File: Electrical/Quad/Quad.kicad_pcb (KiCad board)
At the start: 2 copper layers, 140 x 70 mm, 117 parts, among them J101 01x04, J102 02x04, J103 01x04, J104 01x03, J105 01x03, J106 01x03, J107 01x03, J108 01x03, J109 01x03, J110 01x04, J111 01x04, J112 01x04, J113 01x04, J114 01x03, J115 01x03, J116 01x03, J117 01x03, J201 01x02, J202 01x04, J203 01x03, J204 01x04, J205 01x03, J206 USB_OTG, J207 01x04, J208 01x02, J209 01x04, J210 01x02, J211 01x02, J212 4PostTerm, J213 2PostTerm, J214 2PostTerm, J215 JST_3, J216 2PostTerm, J217 2PostTerm, Q201 FDC6420C, Q202 FDG1024NZ, Q301 FDC6420C, Q401 FDC6420C, U201 TPD4S012, U202 ACS712ELCTR-05B-T, U203 ACS712ELCTR-05B-T, U204 24LC256, U205 LM2576HVS-ADJ, U206 LM2576HVS-ADJ

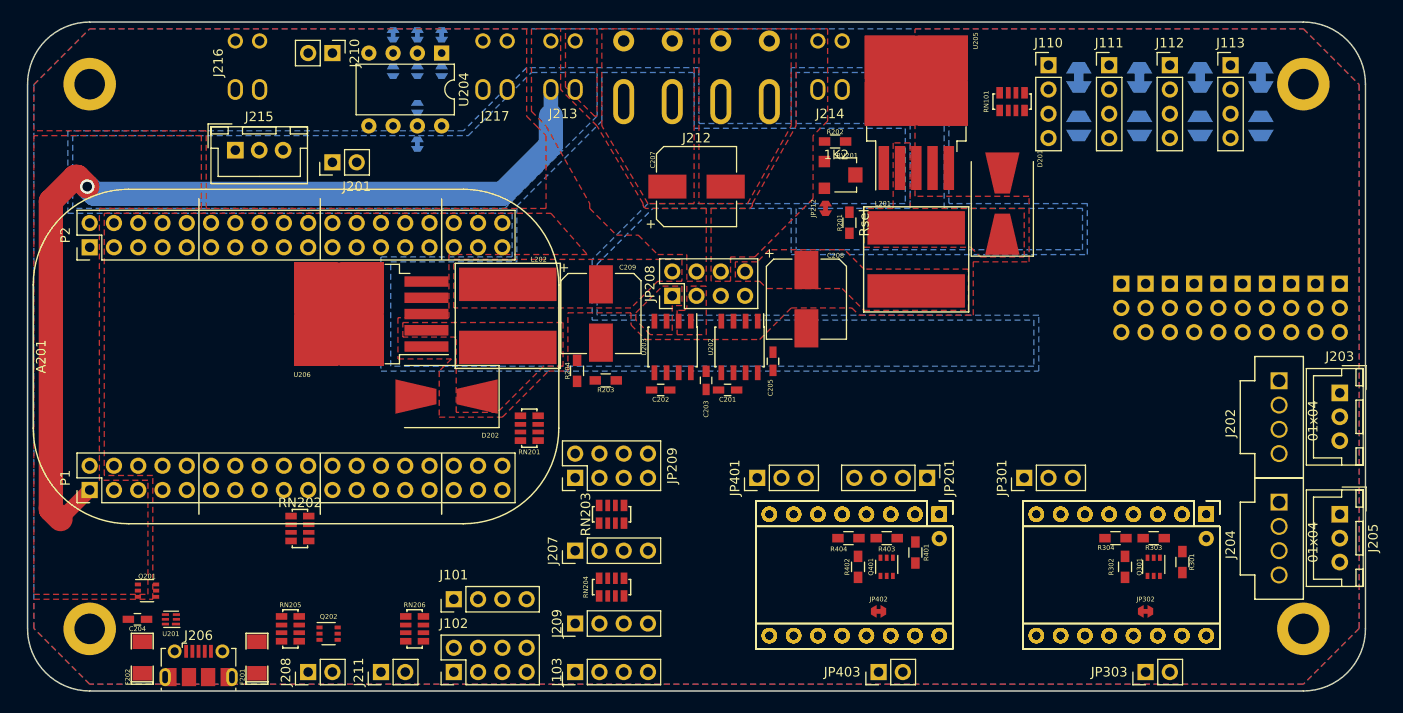
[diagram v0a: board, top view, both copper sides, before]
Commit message: Completed Quad stepper version of the board.
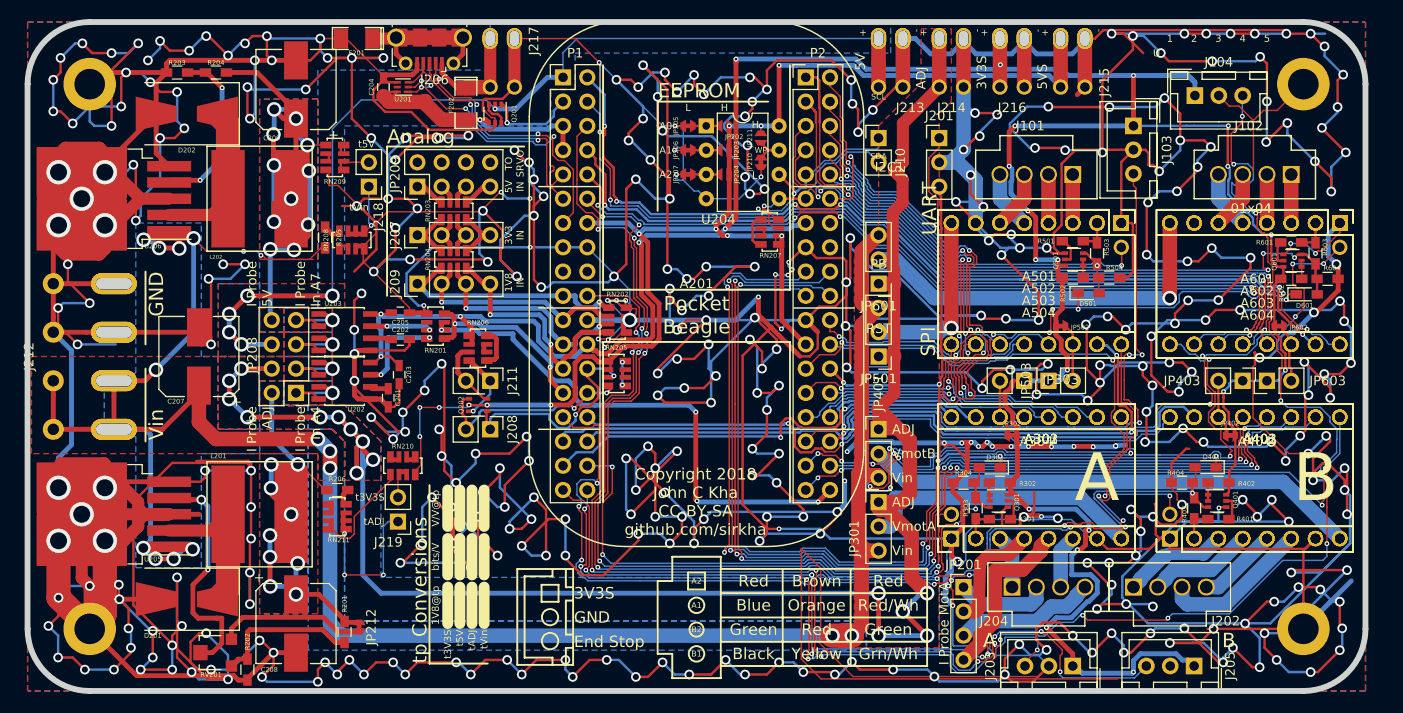
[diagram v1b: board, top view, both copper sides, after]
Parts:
- removed J105, J106, J107, J108, J109, J114, J115, J116, J117: 01x03, footprints:Pin_Header_Straight_1x03_Pitch2.54mm_Blank
- removed J110, J111, J112, J113: 01x04, Pin_Headers:Pin_Header_Straight_1x04_Pitch2.54mm
- removed JP101, JP102, JP103, JP104: JPNC, footprints:JPNC_Large
- removed JP105, JP106, JP107, JP108: JPNO, footprints:JPNO_Large
- removed RN101: 1K2, footprints:R_Array_1206x04
- added A501: Pololu_Breakout_A4988, footprints:Pololu_Breakout-16_15.2x20.3mm, F.Cu at (144.4, 86.0)
- added A502: Pololu_Breakout_DRV8825, footprints:Pololu_Breakout-16_15.2x20.3mm, F.Cu at (144.4, 86.0)
- added A503: Pololu_Breakout_DRV8834, footprints:Pololu_Breakout-16_15.2x20.3mm, F.Cu at (144.4, 86.0)
- added A504: Pololu_Breakout_DRV8880, footprints:Pololu_Breakout-17_15.2x20.3mm, F.Cu at (144.4, 86.0)
- added A601: Pololu_Breakout_A4988, footprints:Pololu_Breakout-16_15.2x20.3mm, F.Cu at (167.3, 86.0)
- added A602: Pololu_Breakout_DRV8825, footprints:Pololu_Breakout-16_15.2x20.3mm, F.Cu at (167.3, 86.0)
- added A603: Pololu_Breakout_DRV8834, footprints:Pololu_Breakout-16_15.2x20.3mm, F.Cu at (167.3, 86.0)
- added A604: Pololu_Breakout_DRV8880, footprints:Pololu_Breakout-17_15.2x20.3mm, F.Cu at (167.3, 86.0)
- added D301: D, footprints:D_0603_HandSoldering, F.Cu at (130.7, 111.6)
- added D401: D, footprints:D_0603_HandSoldering, F.Cu at (153.3, 111.6)
- added D501: D, footprints:D_0603_HandSoldering, F.Cu at (141.0, 93.4)
- added D601: D, footprints:D_0603_HandSoldering, F.Cu at (163.8, 93.5)
- added J218: 01x02, Pin_Headers:Pin_Header_Straight_1x02_Pitch2.54mm, F.Cu at (65.7, 82.2)
- added J219: 01x02, Pin_Headers:Pin_Header_Straight_1x02_Pitch2.54mm, F.Cu at (68.8, 117.3)
- added JP501: 01x03, Pin_Headers:Pin_Header_Straight_1x03_Pitch2.54mm, F.Cu at (119.0, 100.0)
- added JP502: JPNC, footprints:JPNC, F.Cu at (138.1, 96.8)
- added JP503: 01x02, Pin_Headers:Pin_Header_Straight_1x02_Pitch2.54mm, F.Cu at (136.8, 102.5)
- added JP601: 01x03, Pin_Headers:Pin_Header_Straight_1x03_Pitch2.54mm, F.Cu at (119.0, 92.4)
- added JP602: JPNC, footprints:JPNC, F.Cu at (161.0, 96.8)
- added JP603: 01x02, Pin_Headers:Pin_Header_Straight_1x02_Pitch2.54mm, F.Cu at (159.7, 102.5)
- added Q501: FDC6420C, TO_SOT_Packages_SMD:SOT-363_SC-70-6, F.Cu at (139.5, 89.8)
- added Q601: FDC6420C, TO_SOT_Packages_SMD:SOT-363_SC-70-6, F.Cu at (162.4, 90.0)
- added R205: 12K, Resistors_SMD:R_0603_HandSoldering, F.Cu at (61.1, 87.6)
- added R206: 12K, Resistors_SMD:R_0603_HandSoldering, F.Cu at (62.4, 114.0)
- added R501: 22, Resistors_SMD:R_0603_HandSoldering, F.Cu at (139.4, 87.9)
- added R502: 12K, Resistors_SMD:R_0603_HandSoldering, F.Cu at (139.4, 91.7)
- added R503: 1K2, Resistors_SMD:R_0603_HandSoldering, F.Cu at (141.9, 89.2)
- added R504: 12K, Resistors_SMD:R_0603_HandSoldering, F.Cu at (143.2, 91.7)
- added R601: 22, Resistors_SMD:R_0603_HandSoldering, F.Cu at (162.2, 88.1)
- added R602: 12K, Resistors_SMD:R_0603_HandSoldering, F.Cu at (162.2, 91.9)
- added R603: 1K2, Resistors_SMD:R_0603_HandSoldering, F.Cu at (164.8, 89.2)
- added R604: 12K, Resistors_SMD:R_0603_HandSoldering, F.Cu at (166.0, 91.9)
- added RN207: 1K2, footprints:R_Array_1206x04, F.Cu at (107.7, 87.0)
- added RN208: 1K2, footprints:R_Array_1206x04, F.Cu at (63.9, 87.8)
- added RN209: 1K2, footprints:R_Array_1206x04, F.Cu at (62.2, 79.2)
- added RN210: 1K2, footprints:R_Array_1206x04, F.Cu at (69.3, 111.4)
- added RN211: 1K2, footprints:R_Array_1206x04, F.Cu at (62.4, 116.8)
- A301, A302, A303, A401, A402, A403: footprint Modules:Pololu_Breakout-16_15.2x20.3mm -> footprints:Pololu_Breakout-16_15.2x20.3mm
- J101: footprint Pin_Headers:Pin_Header_Straight_1x04_Pitch2.54mm -> footprints:Molex-SL-4POS
- J102: value 02x04 -> 01x04; footprint Pin_Headers:Pin_Header_Straight_2x04_Pitch2.54mm -> footprints:Molex-SL-4POS
- J103: value 01x04 -> 01x03; footprint Pin_Headers:Pin_Header_Straight_1x04_Pitch2.54mm -> Connectors_JST:JST_XH_B03B-XH-A_03x2.50mm_Straight
- J104: footprint footprints:Pin_Header_Straight_1x03_Pitch2.54mm_Blank -> Connectors_JST:JST_XH_B03B-XH-A_03x2.50mm_Straight
- J201: value 01x02 -> 01x03; footprint Pin_Headers:Pin_Header_Straight_1x02_Pitch2.54mm -> Pin_Headers:Pin_Header_Straight_1x03_Pitch2.54mm
- J206: footprint Connectors_USB:USB_Micro-B_Molex-105017-0001 -> footprints:USB_Micro-B_Molex-105017-0001_CircularHoles
- J213, J214, J216, J217, JP202, JP203, JP204, JP205, JP206, JP207, JP210, JP211: moved to F.Cu
- J215: value JST_3 -> 2PostTerm; footprint Connectors_JST:JST_XH_B03B-XH-A_03x2.50mm_Straight -> footprints:TerminalBlock_Custom_1x02.54mm
- moved J102 101.9 mm to (162.2, 81.0), turned to 0 degrees
- moved D201 94.9 mm to (46.7, 125.4), turned to 180 degrees
- moved U205 93.9 mm to (39.0, 116.5), turned to 180 degrees
- moved J215 88.1 mm to (139.4, 69.3)
- moved R202 82.7 mm to (53.0, 132.8), turned to 90 degrees
- moved RV201 82.2 mm to (49.7, 131.0), turned to 90 degrees
- moved J103 81.7 mm to (145.7, 75.9), turned to 270 degrees
- moved J216 80.0 mm to (133.0, 69.3)
- moved J101 78.6 mm to (139.4, 81.0), turned to 0 degrees
- moved L201 73.7 mm to (54.3, 116.5), turned to 0 degrees
- moved J206 70.5 mm to (72.1, 67.0), turned to 180 degrees
- moved J212 69.9 mm to (36.5, 100.0), turned to 270 degrees
- moved R201 68.0 mm to (63.2, 128.8), turned to 270 degrees
- moved F202 67.1 mm to (75.9, 73.6), turned to 270 degrees
- moved A201 65.7 mm to (86.0, 70.8), turned to 0 degrees
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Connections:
- net /Common/usb1_dn renamed /Common/usb1_d-
- net /Common/usb1_dp renamed /Common/usb1_d+
- A201 pad 1.10: /ehrpwm0B -> /gpio0_3
- A201 pad 1.17: Net-(A201-Pad1.17) -> (no net)
- A201 pad 1.18: Net-(A201-Pad1.18) -> (no net)
- A201 pad 1.2: /gpio2_23 -> /pr1_pru1_pru_r30_09
- A201 pad 1.4: /gpio2_25 -> /pr1_pru1_pru_r30_11
- A201 pad 1.8: /ehrpwm0A -> /gpio0_2
- A201 pad 2.1: /ehrpwm1A -> /gpio1_18
- A201 pad 2.10: /Common/gpio1_20 -> /gpio1_20
- A201 pad 2.14: +BATT -> (no net)
- A201 pad 2.16: /Common/batt_temp -> (no net)
- A201 pad 2.24: /gpio1_12 -> /Common/gpio1_12
- A201 pad 2.25: /spi1_d1 -> /gpio1_9
- A201 pad 2.26: Net-(A201-Pad2.26) -> RST
- A201 pad 2.27: /spi1_d0 -> /gpio1_8
- A201 pad 2.28: /gpio3_20 -> /pr1_pru0_pru_r30_06
- A201 pad 2.29: /spi1_sclk -> /gpio0_7
- A201 pad 2.3: /ehrpwm2B -> /gpio0_23
- A201 pad 2.30: /gpio3_17 -> /pr1_pru0_pru_r31_03
- A201 pad 2.31: /spi1_cs1 -> /gpio0_19
- A201 pad 2.32: /gpio3_16 -> /pr1_pru0_pru_r30_02
- A201 pad 2.33: /gpio1_13 -> /pr1_pu0_pru_r30_15
- A201 pad 2.34: /gpio3_19 -> /pr1_pru0_pru_r30_05
- A201 pad 2.35: /gpio2_22 -> /pr1_pru1_pru_r31_08
- A201 pad 2.5: /uart4_rxd -> /gpio0_30
- A201 pad 2.7: /uart4_txd -> /gpio0_31
- A301 pad 10: /Common/gpio2_0 -> /Common/gpio1_27
- A301 pad 11: /Common/gpio0_27 -> /Common/gpio1_26
- A301 pad 12: /Common/gpio1_15 -> /Common/gpio1_25
- A301 pad 13: /Common/gpio2_1 -> /Common/gpio1_28
- A301 pad 14: /Common/StepperB/SLP -> /Common/StepperA/SLP
- A301 pad 15: /Common/pr1_pru1_pru_r30_15 -> /Common/pr1_pru0_pru_r30_04
- A301 pad 16: /Common/pr1_pru1_pru_r30_14 -> /Common/pr1_pru0_pru_r30_01
- A301 pad 2: /Common/StepperB/fault_supply -> /Common/StepperA/fault_supply
- A301 pad 3: /Common/StepperB/A2 -> /Common/StepperA/A2
- A301 pad 4: /Common/StepperB/A1 -> /Common/StepperA/A1
- A301 pad 5: /Common/StepperB/B1 -> /Common/StepperA/B1
- A301 pad 6: /Common/StepperB/B2 -> /Common/StepperA/B2
- A301 pad 8: /Common/StepperB/Vmot -> /Common/StepperA/Vmot
- A301 pad 9: /Common/pr1_pru0_pru_r30_00 -> /Common/pr1_pru0_pru_r30_07
- A302 pad 10: /Common/gpio2_0 -> /Common/gpio1_27
- A302 pad 11: /Common/gpio0_27 -> /Common/gpio1_26
- A302 pad 12: /Common/gpio1_15 -> /Common/gpio1_25
- A302 pad 13: /Common/gpio2_1 -> /Common/gpio1_28
- A302 pad 14: /Common/StepperB/SLP -> /Common/StepperA/SLP
- A302 pad 15: /Common/pr1_pru1_pru_r30_15 -> /Common/pr1_pru0_pru_r30_04
- A302 pad 16: /Common/pr1_pru1_pru_r30_14 -> /Common/pr1_pru0_pru_r30_01
- A302 pad 2: /Common/StepperB/fault_supply -> /Common/StepperA/fault_supply
- A302 pad 3: /Common/StepperB/A2 -> /Common/StepperA/A2
- A302 pad 4: /Common/StepperB/A1 -> /Common/StepperA/A1
- A302 pad 5: /Common/StepperB/B1 -> /Common/StepperA/B1
- A302 pad 6: /Common/StepperB/B2 -> /Common/StepperA/B2
- A302 pad 8: /Common/StepperB/Vmot -> /Common/StepperA/Vmot
- A302 pad 9: /Common/pr1_pru0_pru_r30_00 -> /Common/pr1_pru0_pru_r30_07
- A303 pad 10: /Common/gpio2_0 -> /Common/gpio1_27
- A303 pad 11: /Common/gpio0_27 -> /Common/gpio1_26
- A303 pad 12: /Common/gpio1_15 -> /Common/gpio1_25
- A303 pad 13: /Common/gpio2_1 -> /Common/gpio1_28
- A303 pad 14: /Common/StepperB/SLP -> /Common/StepperA/SLP
- A303 pad 15: /Common/pr1_pru1_pru_r30_15 -> /Common/pr1_pru0_pru_r30_04
- A303 pad 16: /Common/pr1_pru1_pru_r30_14 -> /Common/pr1_pru0_pru_r30_01
- A303 pad 2: /Common/StepperB/fault_supply -> /Common/StepperA/fault_supply
- A303 pad 3: /Common/StepperB/A2 -> /Common/StepperA/A2
- A303 pad 4: /Common/StepperB/A1 -> /Common/StepperA/A1
- A303 pad 5: /Common/StepperB/B1 -> /Common/StepperA/B1
- A303 pad 6: /Common/StepperB/B2 -> /Common/StepperA/B2
- A303 pad 8: /Common/StepperB/Vmot -> /Common/StepperA/Vmot
- A303 pad 9: /Common/pr1_pru0_pru_r30_00 -> /Common/pr1_pru0_pru_r30_07
- A304 pad 10: /Common/gpio2_0 -> /Common/gpio1_27
- A304 pad 11: /Common/gpio0_27 -> /Common/gpio1_26
- A304 pad 12: /Common/gpio1_15 -> /Common/gpio1_25
- A304 pad 13: /Common/gpio2_1 -> /Common/gpio1_28
- A304 pad 14: /Common/StepperB/SLP -> /Common/StepperA/SLP
- A304 pad 15: /Common/pr1_pru1_pru_r30_15 -> /Common/pr1_pru0_pru_r30_04
- A304 pad 16: /Common/pr1_pru1_pru_r30_14 -> /Common/pr1_pru0_pru_r30_01
- A304 pad 17: /Common/gpio1_28 -> /Common/gpio0_26
- A304 pad 2: /Common/StepperB/fault_supply -> /Common/StepperA/fault_supply
- A304 pad 3: /Common/StepperB/A2 -> /Common/StepperA/A2
- A304 pad 4: /Common/StepperB/A1 -> /Common/StepperA/A1
- A304 pad 5: /Common/StepperB/B1 -> /Common/StepperA/B1
- A304 pad 6: /Common/StepperB/B2 -> /Common/StepperA/B2
- A304 pad 8: /Common/StepperB/Vmot -> /Common/StepperA/Vmot
- A304 pad 9: /Common/pr1_pru0_pru_r30_00 -> /Common/pr1_pru0_pru_r30_07
- A401 pad 10: /Common/gpio1_27 -> /Common/gpio2_0
- A401 pad 11: /Common/gpio1_26 -> /Common/gpio0_27
- A401 pad 12: /Common/gpio1_25 -> /Common/gpio1_15
- A401 pad 13: /Common/gpio1_20 -> /Common/gpio2_1
- A401 pad 14: /Common/StepperA/SLP -> /Common/StepperB/SLP
- A401 pad 15: /Common/pr1_pru0_pru_r30_04 -> /Common/pr1_pru1_pru_r30_14
- A401 pad 16: /Common/pr1_pru0_pru_r30_01 -> /Common/pr1_pru1_pru_r30_15
- A401 pad 2: /Common/StepperA/fault_supply -> /Common/StepperB/fault_supply
- A401 pad 3: /Common/StepperA/A2 -> /Common/StepperB/A2
- A401 pad 4: /Common/StepperA/A1 -> /Common/StepperB/A1
- A401 pad 5: /Common/StepperA/B1 -> /Common/StepperB/B1
- A401 pad 6: /Common/StepperA/B2 -> /Common/StepperB/B2
- A401 pad 8: /Common/StepperA/Vmot -> /Common/StepperB/Vmot
- A401 pad 9: /Common/pr1_pru0_pru_r30_07 -> /Common/pr1_pru0_pru_r30_00
- A402 pad 10: /Common/gpio1_27 -> /Common/gpio2_0
- A402 pad 11: /Common/gpio1_26 -> /Common/gpio0_27
- A402 pad 12: /Common/gpio1_25 -> /Common/gpio1_15
- A402 pad 13: /Common/gpio1_20 -> /Common/gpio2_1
- A402 pad 14: /Common/StepperA/SLP -> /Common/StepperB/SLP
- A402 pad 15: /Common/pr1_pru0_pru_r30_04 -> /Common/pr1_pru1_pru_r30_14
- A402 pad 16: /Common/pr1_pru0_pru_r30_01 -> /Common/pr1_pru1_pru_r30_15
- A402 pad 2: /Common/StepperA/fault_supply -> /Common/StepperB/fault_supply
- A402 pad 3: /Common/StepperA/A2 -> /Common/StepperB/A2
- A402 pad 4: /Common/StepperA/A1 -> /Common/StepperB/A1
- A402 pad 5: /Common/StepperA/B1 -> /Common/StepperB/B1
- A402 pad 6: /Common/StepperA/B2 -> /Common/StepperB/B2
- A402 pad 8: /Common/StepperA/Vmot -> /Common/StepperB/Vmot
- A402 pad 9: /Common/pr1_pru0_pru_r30_07 -> /Common/pr1_pru0_pru_r30_00
- A403 pad 10: /Common/gpio1_27 -> /Common/gpio2_0
- A403 pad 11: /Common/gpio1_26 -> /Common/gpio0_27
- A403 pad 12: /Common/gpio1_25 -> /Common/gpio1_15
- A403 pad 13: /Common/gpio1_20 -> /Common/gpio2_1
- A403 pad 14: /Common/StepperA/SLP -> /Common/StepperB/SLP
- A403 pad 15: /Common/pr1_pru0_pru_r30_04 -> /Common/pr1_pru1_pru_r30_14
- A403 pad 16: /Common/pr1_pru0_pru_r30_01 -> /Common/pr1_pru1_pru_r30_15
- A403 pad 2: /Common/StepperA/fault_supply -> /Common/StepperB/fault_supply
- A403 pad 3: /Common/StepperA/A2 -> /Common/StepperB/A2
- A403 pad 4: /Common/StepperA/A1 -> /Common/StepperB/A1
- A403 pad 5: /Common/StepperA/B1 -> /Common/StepperB/B1
- A403 pad 6: /Common/StepperA/B2 -> /Common/StepperB/B2
- A403 pad 8: /Common/StepperA/Vmot -> /Common/StepperB/Vmot
- A403 pad 9: /Common/pr1_pru0_pru_r30_07 -> /Common/pr1_pru0_pru_r30_00
- A404 pad 10: /Common/gpio1_27 -> /Common/gpio2_0
- A404 pad 11: /Common/gpio1_26 -> /Common/gpio0_27
- A404 pad 12: /Common/gpio1_25 -> /Common/gpio1_15
- A404 pad 13: /Common/gpio1_20 -> /Common/gpio2_1
- A404 pad 14: /Common/StepperA/SLP -> /Common/StepperB/SLP
- A404 pad 15: /Common/pr1_pru0_pru_r30_04 -> /Common/pr1_pru1_pru_r30_14
- A404 pad 16: /Common/pr1_pru0_pru_r30_01 -> /Common/pr1_pru1_pru_r30_15
- A404 pad 17: /Common/gpio0_26 -> /Common/gpio1_12
- A404 pad 2: /Common/StepperA/fault_supply -> /Common/StepperB/fault_supply
- A404 pad 3: /Common/StepperA/A2 -> /Common/StepperB/A2
- A404 pad 4: /Common/StepperA/A1 -> /Common/StepperB/A1
- A404 pad 5: /Common/StepperA/B1 -> /Common/StepperB/B1
- A404 pad 6: /Common/StepperA/B2 -> /Common/StepperB/B2
- A404 pad 8: /Common/StepperA/Vmot -> /Common/StepperB/Vmot
- A404 pad 9: /Common/pr1_pru0_pru_r30_07 -> /Common/pr1_pru0_pru_r30_00
- C204 pad 1: Net-(C204-Pad1) -> /Common/usb1_vbus
- F202 pad 1: Net-(F202-Pad1) -> /Common/usb1_5V
- F202 pad 2: Net-(C204-Pad1) -> /Common/usb1_vbus
- J101 pad 1: GND -> /StepperC/A2
- J101 pad 2: /uart4_txd -> /StepperC/A1
- J101 pad 3: /uart4_rxd -> /StepperC/B2
- J101 pad 4: 3V3S -> /StepperC/B1
- J102 pad 1: /spi1_d1 -> /StepperD/A2
- J102 pad 2: 3V3S -> /StepperD/A1
- J102 pad 3: /spi1_cs1 -> /StepperD/B2
- J102 pad 4: GND -> /StepperD/B1
- J103 pad 1: /ehrpwm2B -> 3V3S
- J103 pad 2: /ehrpwm1A -> GND
- J103 pad 3: /ehrpwm0B -> /pr1_pru0_pru_r31_03
- J104 pad 1: GND -> 3V3S
- J104 pad 2: 3V3S -> GND
- J104 pad 3: /gpio1_12 -> /pr1_pru1_pru_r31_08
- J201 pad 2: Net-(A201-Pad2.26) -> GND
- J206 pad 1: Net-(F202-Pad1) -> /Common/usb1_5V
- J208 pad 1: /Common/i2c2_scl -> /Common/i2c2_sda
- J208 pad 2: /Common/i2c2_sda -> /Common/i2c2_scl
- J210 pad 1: /Common/i2c1_sda -> /Common/i2c1_scl
- J210 pad 2: /Common/i2c1_scl -> /Common/i2c1_sda
- J215 pad 1: +BATT -> 5VS
- J215 pad 2: /Common/batt_temp -> GND
- J216 pad 1: 5VS -> 3V3S
- J217 pad 1: 3V3S -> /Common/usb1_5V
- JP208 pad b1: /Common/IP_5V -> /Common/IP_vadj
- JP208 pad b2: +5V -> Vadj
- JP208 pad b3: Vadj -> +5V
- JP208 pad b4: /Common/IP_vadj -> /Common/IP_5V
- JP209 pad b1: /ain_0 -> GND
- JP209 pad b2: /ain_1 -> GND
- JP209 pad b3: /ain_2 -> GND
- JP209 pad b4: /ain_3 -> GND
- JP301 pad 1: Vin -> Vadj
- JP301 pad 2: /Common/StepperB/Vmot -> /Common/StepperA/Vmot
- JP301 pad 3: Vadj -> Vin
- JP302 pad 1: /Common/StepperB/SLP -> /Common/StepperA/SLP
- JP303 pad 2: /Common/StepperB/SLP -> /Common/StepperA/SLP
- JP401 pad 1: Vin -> Vadj
- JP401 pad 2: /Common/StepperA/Vmot -> /Common/StepperB/Vmot
- JP401 pad 3: Vadj -> Vin
- JP402 pad 1: /Common/StepperA/SLP -> /Common/StepperB/SLP
- JP403 pad 2: /Common/StepperA/SLP -> /Common/StepperB/SLP
- Q201 pad 4: Net-(C204-Pad1) -> /Common/usb1_vbus
- Q202 pad 3: Net-(J211-Pad2) -> Net-(J211-Pad1)
- Q202 pad 6: Net-(J211-Pad1) -> Net-(J211-Pad2)
- Q301 pad 3: /Common/gpio0_4 -> /Common/gpio0_5
- Q401 pad 3: /Common/gpio0_5 -> /Common/gpio0_4
- R301 pad 1: /Common/StepperB/fault_supply -> /Common/StepperA/fault_supply
- R303 pad 1: /Common/gpio0_4 -> /Common/gpio0_5
- R303 pad 2: /Common/StepperB/fault_supply -> /Common/StepperA/fault_supply
- R304 pad 1: /Common/gpio0_4 -> /Common/gpio0_5
- R401 pad 1: /Common/StepperA/fault_supply -> /Common/StepperB/fault_supply
- R403 pad 1: /Common/gpio0_5 -> /Common/gpio0_4
- R403 pad 2: /Common/StepperA/fault_supply -> /Common/StepperB/fault_supply
- R404 pad 1: /Common/gpio0_5 -> /Common/gpio0_4
- RN201 pad 6: Net-(RN201-Pad6) -> (no net)
- RN205 pad 1: Net-(RN205-Pad1) -> 3V3S
- RN205 pad 2: Net-(RN205-Pad2) -> 3V3S
- RN205 pad 3: Net-(RN205-Pad2) -> /Common/i2c2_sda
- RN205 pad 4: Net-(RN205-Pad1) -> /Common/i2c2_scl
- RN205 pad 5: /Common/i2c2_sda -> Net-(RN205-Pad5)
- RN205 pad 6: /Common/i2c2_scl -> Net-(RN205-Pad6)
- RN205 pad 7: 3V3S -> Net-(RN205-Pad6)
- RN205 pad 8: 3V3S -> Net-(RN205-Pad5)
- RN206 pad 3: Net-(J211-Pad1) -> Net-(J211-Pad2)
- RN206 pad 4: Net-(J211-Pad2) -> Net-(J211-Pad1)
- U201 pad 5: Net-(U201-Pad5) -> (no net)
- U201 pad 6: Net-(C204-Pad1) -> /Common/usb1_vbus
- U202 pad 1: Net-(JP208-Pada4) -> Net-(JP208-Pada2)
- U202 pad 2: Net-(JP208-Pada4) -> Net-(JP208-Pada2)
- U202 pad 3: Net-(JP208-Pada3) -> Net-(JP208-Pada1)
- U202 pad 4: Net-(JP208-Pada3) -> Net-(JP208-Pada1)
- U203 pad 1: Net-(JP208-Pada2) -> Net-(JP208-Pada4)
- U203 pad 2: Net-(JP208-Pada2) -> Net-(JP208-Pada4)
- U203 pad 3: Net-(JP208-Pada1) -> Net-(JP208-Pada3)
- U203 pad 4: Net-(JP208-Pada1) -> Net-(JP208-Pada3)
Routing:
- net GND: track 0.00 -> 2829.8 mm, vias 0 -> 419
- net 3V3S: track 0.00 -> 355.2 mm, vias 0 -> 31
- net Vin: track 0.00 -> 243.9 mm, vias 0 -> 16
- net Vadj: track 0.00 -> 204.5 mm, vias 0 -> 15
- net 5VS: track 0.00 -> 134.2 mm, vias 0 -> 6
- net /Common/gpio0_4: track 0.00 -> 129.0 mm, vias 0 -> 10
- net RST: track 0.00 -> 127.3 mm, vias 0 -> 10
- net /Common/pr1_pru0_pru_r30_00: track 0.00 -> 119.8 mm, vias 0 -> 10
- net /pr1_pru1_pru_r31_08: track 0.00 -> 118.9 mm, vias 0 -> 10
- net /Common/gpio2_0: track 0.00 -> 114.7 mm, vias 0 -> 6
- net /Common/pr1_pru0_pru_r31_16: track 0.00 -> 112.8 mm, vias 0 -> 9
- net /Common/gpio1_15: track 0.00 -> 111.8 mm, vias 0 -> 6
- net /Common/gpio0_27: track 0.00 -> 110.6 mm, vias 0 -> 6
- net /Common/gpio2_1: track 0.00 -> 108.7 mm, vias 0 -> 5
- net /Common/gpio0_5: track 0.00 -> 107.8 mm, vias 0 -> 8
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- added copper zone on B.Cu, net /Common/IP_5V
- added copper zone on B.Cu, net /Common/IP_vadj
- added copper zone on B.Cu, net Net-(JP208-Pada1)
- added copper zone on B.Cu, net Net-(JP208-Pada2)
- added copper zone on B.Cu, net Net-(JP208-Pada3)
- added copper zone on F.Cu, net Net-(JP208-Pada3)
- added copper zone on B.Cu, net Net-(JP208-Pada4)
- added copper zone on F.Cu, net Net-(JP208-Pada4)
- removed copper zone on F.Cu, net Net-(D201-Pad1)
- removed copper zone on F.Cu, net Net-(D202-Pad1)
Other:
- outline, holes or cut-outs redrawn
- net class Default: clearance 0.254 -> 0.1524
- rule trace_clearance: 0.254 -> 0.1524
- rule trace_min: 0.1524 -> 0.152375
- board text added: "+"
- board text added: "-"
- board text added: "1"
- board text added: "1V8 IN"
- board text added: "1V8@tp"
- board text added: "2"
- board text added: "3"
- board text added: "3V3 IN"
- board text added: "3V3S"
- board text added: "4"
- board text added: "5"
- board text added: "5V"
- board text added: "5V IN"
- board text added: "5VS"
- board text added: "A"
- board text added: "A0"
- board text added: "A1"
- board text added: "A2"
- board text added: "ADJ"
- board text added: "Analog"
- board text added: "B"
- board text added: "B1"
- board text added: "B2"
- board text added: "Black"
- board text added: "Blue"
- board text added: "Brown"
- board text added: "Copyright 2018 John C Kha CC-BY-SA github.com/sirkha"
- board text added: "EEPROM"
- board text added: "End Stop"
- board text added: "GND"
- board text added: "Green"
- board text added: "Grn/Wh"
- board text added: "H"
- board text added: "I Probe 5V"
- board text added: "I Probe ADJ"
- board text added: "I Probe In A4"
- board text added: "I Probe In A7"
- board text added: "I Probe MotA"
- board text added: "I2C1"
- board text added: "L"
- board text added: "Orange"
- board text added: "PB"
- board text added: "Pocket Beagle"
- board text added: "RST"
- board text added: "Red"
- board text added: "Red/Wh"
- board text added: "SCL"
- board text added: "SDA"
- board text added: "SPI"
- board text added: "TO SRVO"
- board text added: "U"
- board text added: "UART"
- board text added: "V/V@tp"
- board text added: "Vin"
- board text added: "VmotA"
- board text added: "VmotB"
- board text added: "WP"
- board text added: "Yellow"
- board text added: "bits/V"
- board text added: "t3V3S"
- board text added: "t5V"
- board text added: "tADJ"
- board text added: "tVin"
- board text added: "tp Conversions"

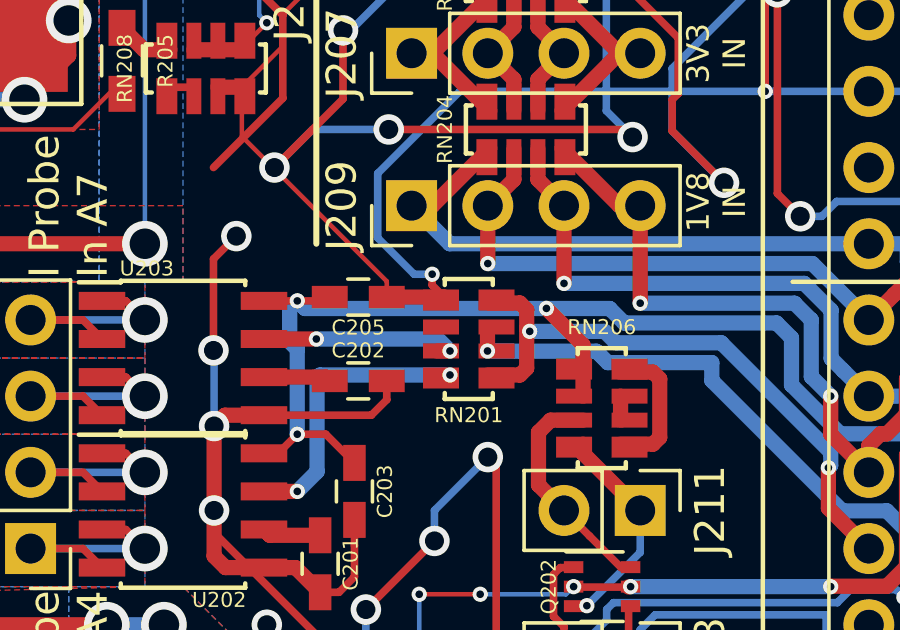
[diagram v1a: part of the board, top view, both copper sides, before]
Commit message: fixed unconnected pad 6 on RN201
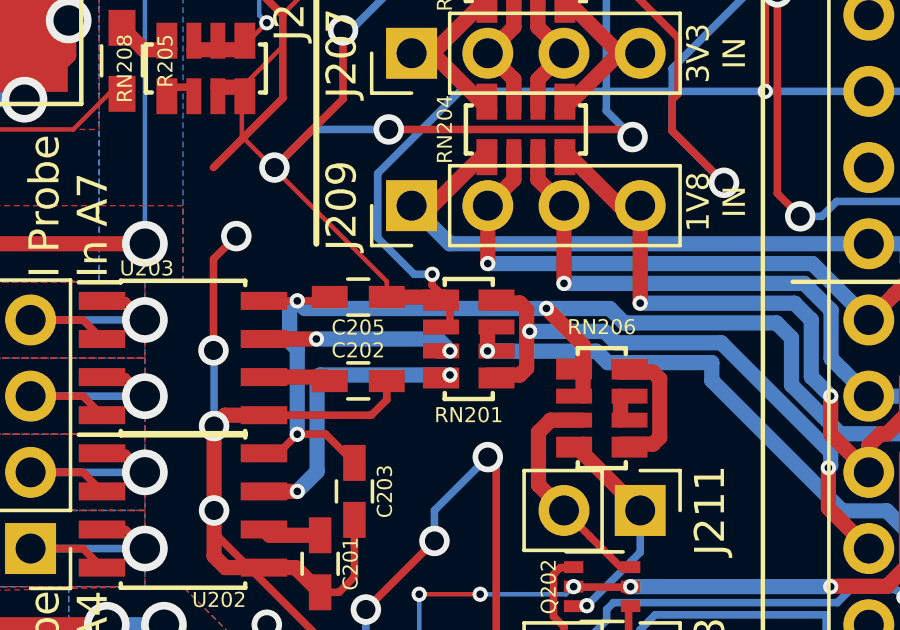
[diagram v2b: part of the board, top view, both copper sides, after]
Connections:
- RN201 pad 6: (no net) -> GND
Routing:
- net GND: track 2829.8 -> 2830.6 mm
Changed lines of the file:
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@@
 (kicad_pcb (version 4) (host pcbnew 4.0.7)
   (general
-    (links 605)
-    (no_connects 0)
-    (area 13.150001 57.061 175.794287 147.700001)
+    (links 606)
+    (no_connects 1)
+    (area 29.695199 64.695199 170.304801 135.304801)
     (thickness 1.6)
     (drawings 192)
-    (tracks 5408)
+    (tracks 5409)
     (zones 0)
     (modules 132)
@@
     (pad 3 smd rect (at 0.4 0.625 90) (size 0.5 1.2) (drill (offset 0 0.3)) (layers F.Cu F.Paste F.Mask)
       (net 81 /Common/ain7))
-    (pad 6 smd rect (at 0.4 -0.625 270) (size 0.5 1.2) (drill (offset 0 0.3)) (layers F.Cu F.Paste F.Mask))
+    (pad 6 smd rect (at 0.4 -0.625 270) (size 0.5 1.2) (drill (offset 0 0.3)) (layers F.Cu F.Paste F.Mask)
+      (net 1 GND))
     (pad 7 smd rect (at -0.4 -0.625 270) (size 0.5 1.2) (drill (offset 0 0.3)) (layers F.Cu F.Paste F.Mask)
       (net 94 "Net-(RN201-Pad7)"))
@@
   (gr_arc (start 36.5 128.5) (end 36.5 135) (angle 90) (layer Edge.Cuts) (width 0.6096))
   (gr_arc (start 163.5 128.5) (end 170 128.5) (angle 90) (layer Edge.Cuts) (width 0.6096))
+  (segment (start 72.07 95.625) (end 72.07 96.425) (width 0.254) (layer F.Cu) (net 1))
   (segment (start 134.25444 116.7767) (end 137.65296 116.7767) (width 0.254) (layer B.Cu) (net 1))
   (segment (start 137.65296 116.7767) (end 137.8079 116.93164) (width 0.254) (layer B.Cu) (net 1))
